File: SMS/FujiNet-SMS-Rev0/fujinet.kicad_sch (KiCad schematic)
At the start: 14 parts, among them J3 microSD, SW3 S3_RST, SW4 S3_BOOT, U9 ESP32-S3-WROOM-1-N16R8

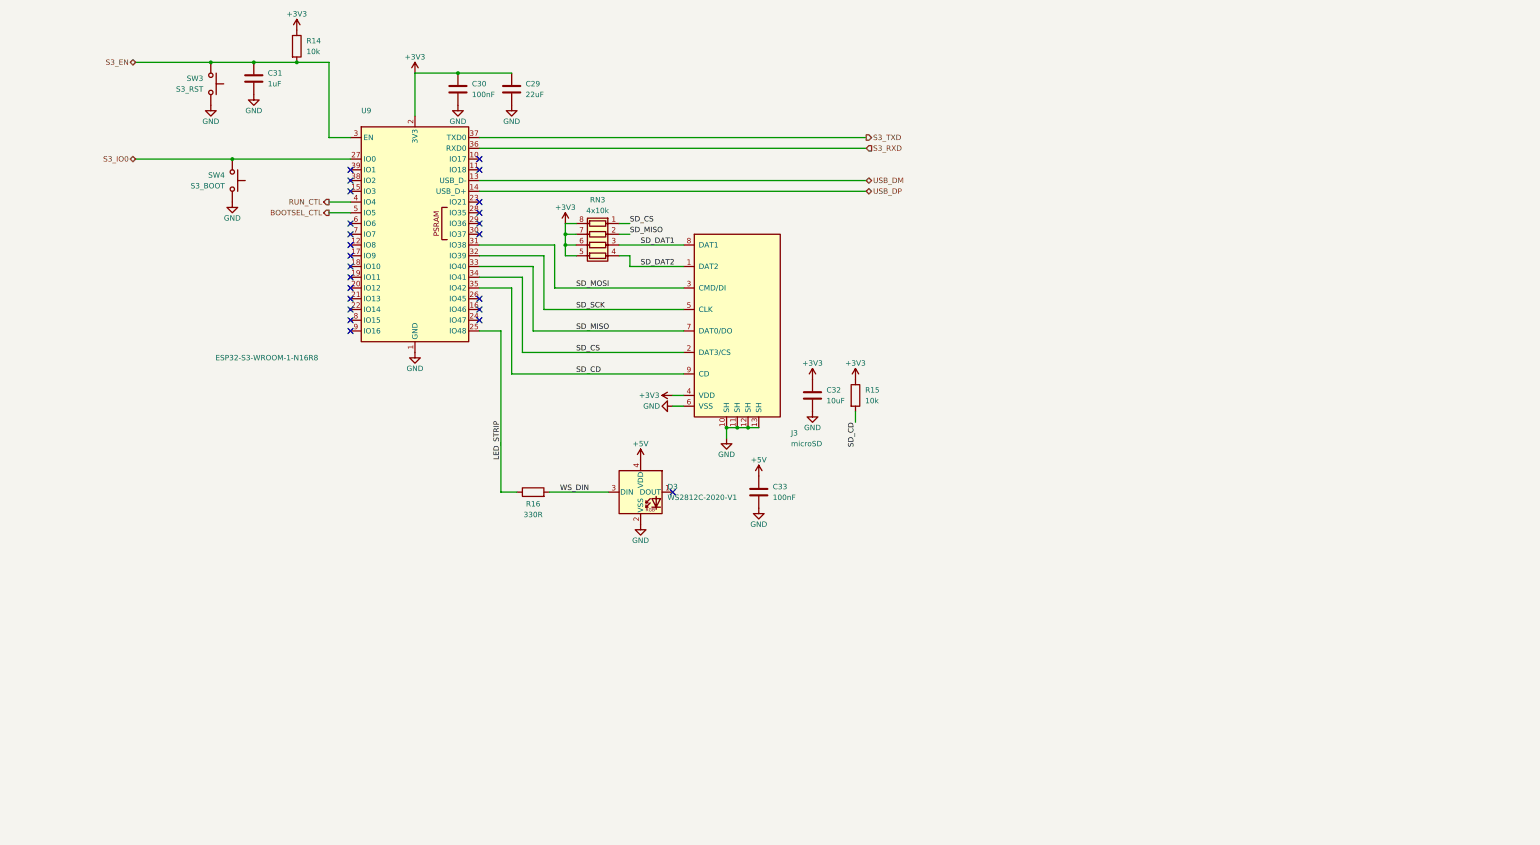
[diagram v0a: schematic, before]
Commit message: SMS Rev0 v2: co-designed floorplan, region sheets, E9 pull-downs, frozen refs and nets
Floorplan study (docs/floorplan-study.md): the SMS edge is the JEDEC
32-pin memory pinout unrolled, so SRAM0 standing upright in the ROM spot
takes A0-A12 / D0-D7 / GND with no crossing.  gen_pcb.sram0_fanin draws
that fan-in locked (funnel, two corner wraps, B-finger jog vias, escape
vias for CE# and OE#).  Four candidates scored and trial-routed in
parallel; P3 (RP2354B straight north of SRAM0, SRAM1 west, glue east over
the strobes) routes best (45 unrouted after 4 passes vs 50 for the first
layout) and reads straight across on the schematic page.

- placement.py: candidates as blocks; the RP2354B + ring as a rigid macro
  (turns as a whole, dvdd_island turns with it); per-variant In4 +5V
  island polygon; label area for the shell
- design.py: sheets are board regions (cart-bus, rp-core, fujinet, usb,
  power); the RP2354B as a two-unit symbol (GPIO on cart-bus, core on
  rp-core); resistor packs one unit per resistor; RP2350-E9 4.7k
  pull-downs on GAME/LOAD/RAM_WE/MBOX/SA19 (check_nets asserts <= 8.2k);
  bring-up pads (CE, OE, WE, PWR_OK, rails, DVDD)
- geographic references (tools/annotate.py -> tools/refs.lock); net names
  frozen in tools/nets.lock (gen_sch fails if a redraw changes one)
- sch_draft.py: an every-pin-labelled draft of the final hierarchy so the
  board is built while the sheets are drawn; sch_draw lint for wired
  sheets (one piece per net, no 4-way junctions, wires clear of text,
  crossing count); sch_place.py mirror check
- check_parts_inside: footprint keep-outs (the S3 antenna bars parts)
- shell: RESET plunger redesigned (captive flange under the guide, stem
  on the TS-1187A actuator, travel asserts, interference part)

ERC 0, parity 126/126, check_nets 442/442, check_glue 8192/8192.
Board placed, not routed yet.

Co-Authored-By: Claude Opus 5.5 <noreply@anthropic.com>
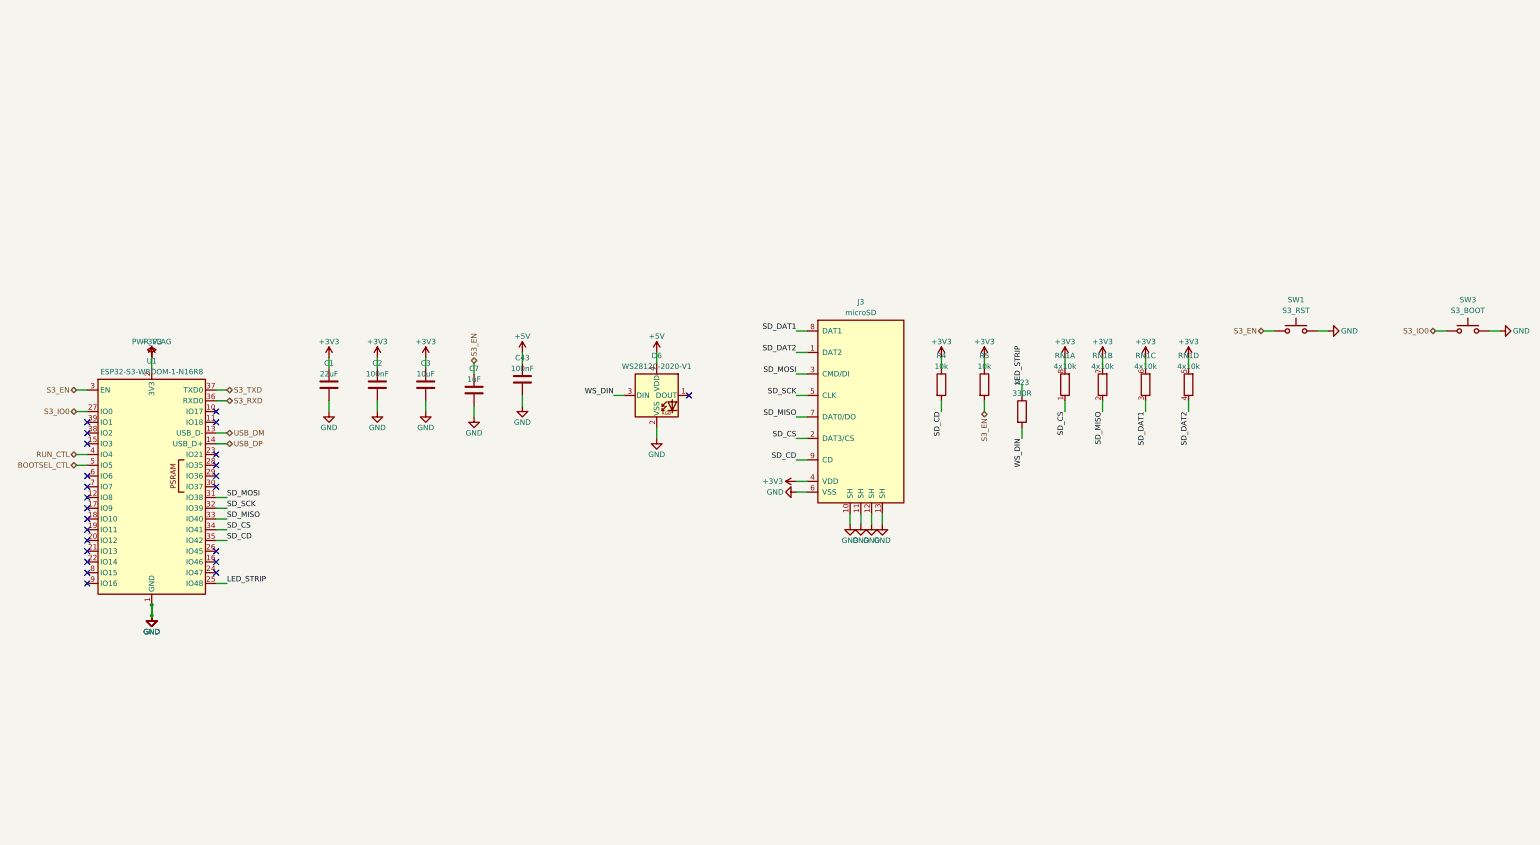
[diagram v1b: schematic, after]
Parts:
- removed C29: 22uF, FujiNet-SMS:C_0805_2012Metric, symbol Device:C
- removed C30, C33: 100nF, FujiNet-SMS:C_0603_1608Metric, symbol Device:C
- removed C31: 1uF, FujiNet-SMS:C_0603_1608Metric, symbol Device:C
- removed C32: 10uF, FujiNet-SMS:C_0603_1608Metric, symbol Device:C
- removed D3: WS2812C-2020-V1, FujiNet-SMS:LED_WS2812B-2020_PLCC4_2.0x2.0mm, symbol LED:WS2812B-2020
- removed R14, R15: 10k, FujiNet-SMS:R_0603_1608Metric, symbol Device:R
- removed R16: 330R, FujiNet-SMS:R_0603_1608Metric, symbol Device:R
- removed RN3: 4x10k, FujiNet-SMS:R_Array_Convex_4x0603, symbol Device:R_Pack04
- removed SW4: S3_BOOT, FujiNet-SMS:SW_SPST_TS-1187A, symbol Switch:SW_Push
- removed U9: ESP32-S3-WROOM-1-N16R8, FujiNet-SMS:ESP32-S3-WROOM-1, symbol RF_Module:ESP32-S3-WROOM-1
- added C1: 22uF, FujiNet-SMS:C_0805_2012Metric, symbol Device:C
- added C2, C43: 100nF, FujiNet-SMS:C_0603_1608Metric, symbol Device:C
- added C3: 10uF, FujiNet-SMS:C_0603_1608Metric, symbol Device:C
- added C7: 1uF, FujiNet-SMS:C_0603_1608Metric, symbol Device:C
- added D6: WS2812C-2020-V1, FujiNet-SMS:LED_WS2812B-2020_PLCC4_2.0x2.0mm, symbol LED:WS2812B-2020
- added R23: 330R, FujiNet-SMS:R_0603_1608Metric, symbol Device:R
- added R4, R5: 10k, FujiNet-SMS:R_0603_1608Metric, symbol Device:R
- added RN1: 4x10k, FujiNet-SMS:R_Array_Convex_4x0603, symbol Device:R_Pack04_Split
- added SW1: S3_RST, FujiNet-SMS:SW_SPST_TS-1187A, symbol Switch:SW_Push
- added U1: ESP32-S3-WROOM-1-N16R8, FujiNet-SMS:ESP32-S3-WROOM-1, symbol RF_Module:ESP32-S3-WROOM-1
- SW3: value S3_RST -> S3_BOOT
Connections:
- net +3V3: now also C1.1, C2.1, C3.1, R4.1, R5.1, RN1.5 (R4.2), RN1.6 (R3.2), RN1.7 (R2.2), RN1.8 (R1.2), U1.2 (3V3)
- net +5V: now also C43.1, D6.4 (VDD)
- net BOOTSEL_CTL: now also U1.5 (IO5)
- net GND: now also C1.2, C2.2, C3.2, C43.2, C7.2, D6.2 (VSS), SW1.2, U1.1 (GND), U1.40 (GND), U1.41 (GND)
- net LED_STRIP: now also R23.1, U1.25 (IO48)
- net RUN_CTL: now also U1.4 (IO4)
- net S3_EN: now also C7.1, R5.2, SW1.1, U1.3 (EN); no longer SW3.1
- net S3_IO0: now also SW3.1, U1.27 (IO0)
- net S3_RXD: now also U1.36 (RXD0)
- net S3_TXD: now also U1.37 (TXD0)
- net SD_CD: now also R4.2, U1.35 (IO42)
- net SD_CS: now also RN1.1 (R1.1), U1.34 (IO41)
- net SD_DAT1: now also RN1.3 (R3.1)
- net SD_DAT2: now also RN1.4 (R4.1)
- net SD_MISO: now also RN1.2 (R2.1), U1.33 (IO40)
- net SD_MOSI: now also U1.31 (IO38)
- net SD_SCK: now also U1.32 (IO39)
- net USB_DM: now also U1.13 (USB_D-)
- net USB_DP: now also U1.14 (USB_D+)
- net WS_DIN: now also D6.3 (DIN), R23.2
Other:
- title: FujiNet SMS Rev0 - ESP32-S3, microSD, status LED -> FujiNet SMS Rev0 - FujiNet: ESP32-S3, microSD, status LED

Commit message: SMS Rev0 v2: redraw every sheet to mirror the board
Each sheet is now hand-placed in tools/sch_layout.py from where its parts
sit on the board, turned so the edge fingers face left (south -> left,
north -> right, west -> top, east -> bottom), and every connection on a
sheet is a wire:

- rp-core: the RP2354B core unit with its decoupling ring at the pins, the
  regulator corner, the crystal, SWD, RUN / BOOTSEL and the RESET diode
  (planar).
- fujinet: a functional ESP32-S3 symbol, EN / BOOT, the WS2812, and the
  microSD's SPI lines stepping into the socket with the pull-ups between
  them (planar).
- usb: a functional USB-C symbol, the CP2102N mirrored to face the
  receptacle, and the auto-program pair.  This page has one crossing, which
  cannot be avoided: RTS and DTR sit side by side on the bridge and each
  feeds the base of one transistor and the emitter of the other.
- power: the CONS_5V / VBUS OR on one +5V line, the LDO above it, the buck
  below it, and the rail PWR_FLAGs grouped together (planar).
- root: the board outline at 2:1, turned the same way, with each sheet's
  block at its region and the nine signals between sheets wired without a
  crossing; notes cover the stack-up and the firmware contract.

Gates: gen_sch.py checks the mirror (Kendall tau >= 0.85 per axis for the
major parts, multi-unit packages counted at the centre of their units,
parts within 5 mm on the board counted as level; every sheet is at
1.00 / 1.00) and a crossing budget per sheet (cart-bus 75, usb 1,
others 0).  ERC is 0 at all severities, netlist parity holds, the net
names equal tools/nets.lock, check_nets passes 442/442, check_glue
8192/8192, and edge_orientation passes.

Co-Authored-By: Claude Opus 5.5 <noreply@anthropic.com>
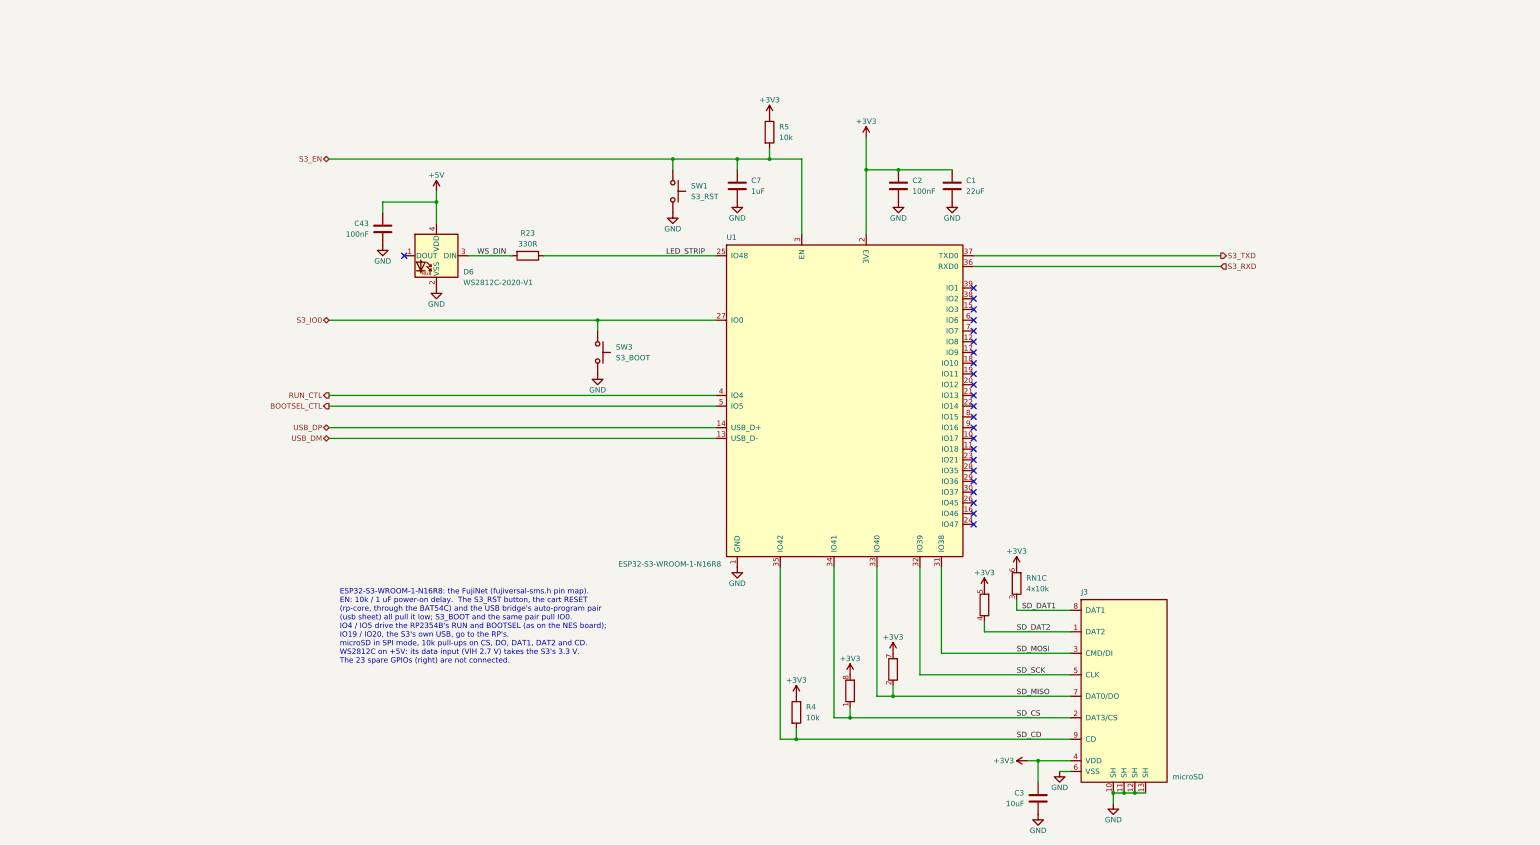
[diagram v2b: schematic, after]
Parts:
- U1: symbol RF_Module:ESP32-S3-WROOM-1 -> FujiNet-SMS:ESP32-S3-WROOM-1_Fn
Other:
- note added: "ESP32-S3-WROOM-1-N16R8: the FujiNet (fujiversal-sms.h pin map). EN: 10k / 1 uF power-on delay. The S3_RST button, the cart RESET (rp-core, through the BAT54C) and the USB bridge's auto-program pair (usb sheet) all pull it low; S3_BOOT and the same pair pull IO0. IO4 / IO5 drive the RP2354B's RUN and BOOTSEL (as on the NES board); IO19 / IO20, the S3's own USB, go to the RP's. microSD in SPI mode,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"
- title: FujiNet SMS Rev0 - FujiNet: ESP32-S3, microSD, status LED -> FujiNet SMS Rev0 - FujiNet: ESP32-S3, microSD, LED
- moved on the sheet: C1, C2, C3, C43, C7, D6, J3, R23, R4, R5, RN1C, SW1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
